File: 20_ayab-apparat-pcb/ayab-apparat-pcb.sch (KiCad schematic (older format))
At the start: 1 part

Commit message: added atmega schematic
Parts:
- removed IC?: ATMEGA328-P, DIL28, symbol ATMEGA328-P
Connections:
- wire segments 0 -> 5
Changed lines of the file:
@@
 $Descr A4 11693 8268
 encoding utf-8
-Sheet 1 2
+Sheet 1 3
 Title ""
 Date ""
@@
 Comment4 ""
 $EndDescr
-$Comp
-L ATMEGA328-P IC?
-U 1 1 52E1499B
-P 3050 2700
-F 0 "IC?" H 2300 3950 40  0000 L BNN
-F 1 "ATMEGA328-P" H 3450 1300 40  0000 L BNN
-F 2 "DIL28" H 3050 2700 30  0000 C CIN
-F 3 "" H 3050 2700 60  0000 C CNN
-	1    3050 2700
-	1    0    0    -1
-$EndComp
 $Sheet
-S 7750 3300 1200 900
+S 4600 2050 950  1050
 U 52E14CBB
 F0 "machine_interface" 50
 F1 "machine_interface.sch" 50
-F2 "EOL_L" I L 7750 3650 60
+F2 "EOL_L" I L 4600 2900 60
+F3 "SDA" I L 4600 2150 60
+F4 "SCL" I L 4600 2250 60
+F5 "EOL_R" I L 4600 3000 60
+F6 "BELTSHIFT" I L 4600 2750 60
+F7 "V1" I L 4600 2550 60
+F8 "V2" I L 4600 2650 60
 $EndSheet
+$Sheet
+S 3250 2100 800  900
+U 52E804E1
+F0 "atmega" 50
+F1 "atmega.sch" 50
+F2 "V2" I R 4050 2650 60
+F3 "V1" I R 4050 2550 60
+F4 "BELTSHIFT" I R 4050 2750 60
+F5 "SCL" I R 4050 2250 60
+F6 "SDA" I R 4050 2150 60
+$EndSheet
+Wire Wire Line
+	4050 2550 4600 2550
+Wire Wire Line
+	4050 2650 4600 2650
+Wire Wire Line
+	4050 2750 4600 2750
+Wire Wire Line
+	4050 2250 4600 2250
+Wire Wire Line
+	4050 2150 4600 2150
 $EndSCHEMATC

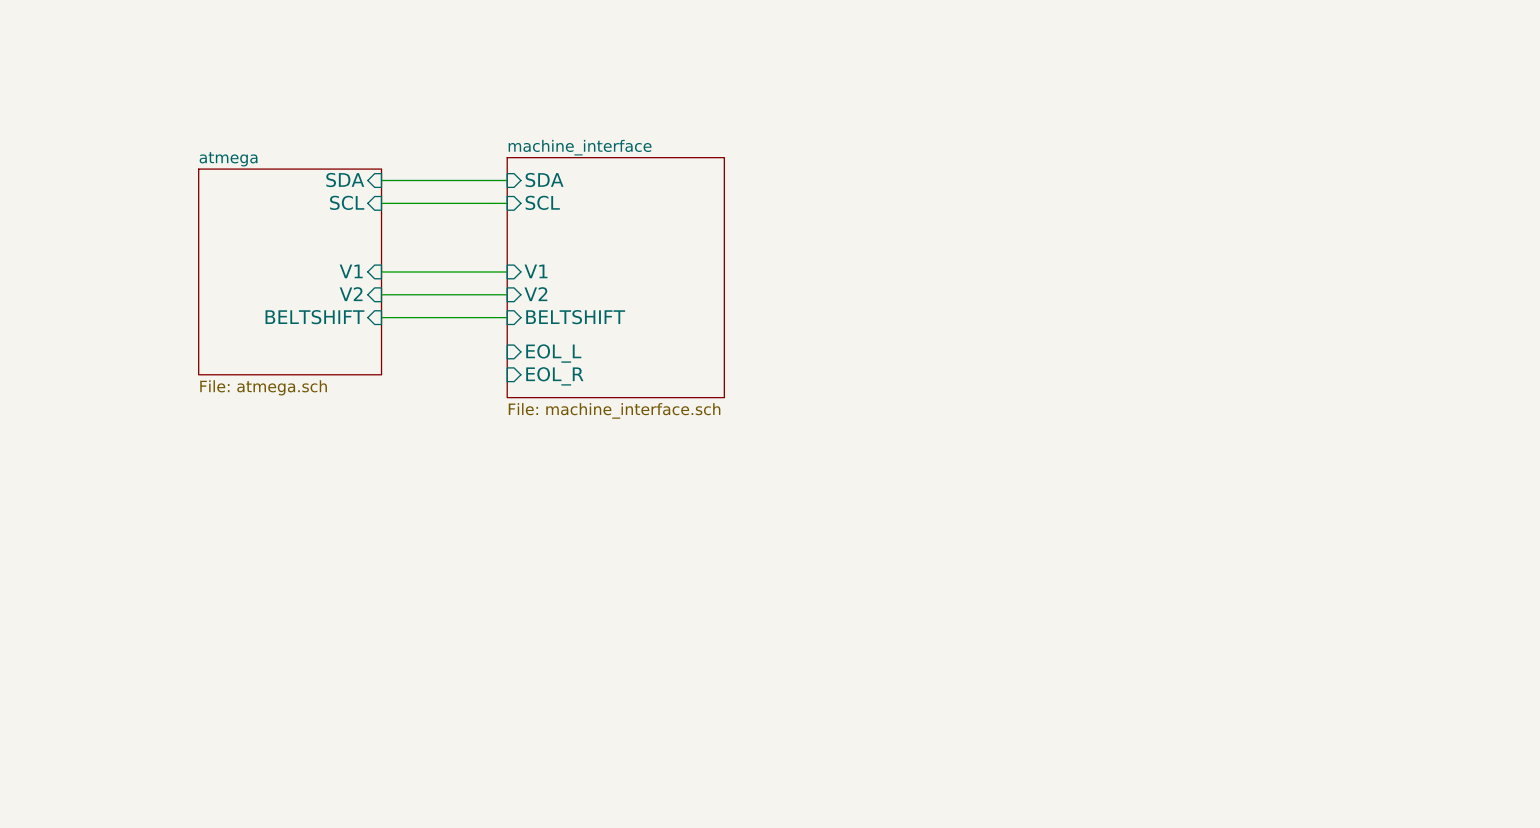
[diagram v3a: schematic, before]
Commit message: schematic structure finished -> todo add part values
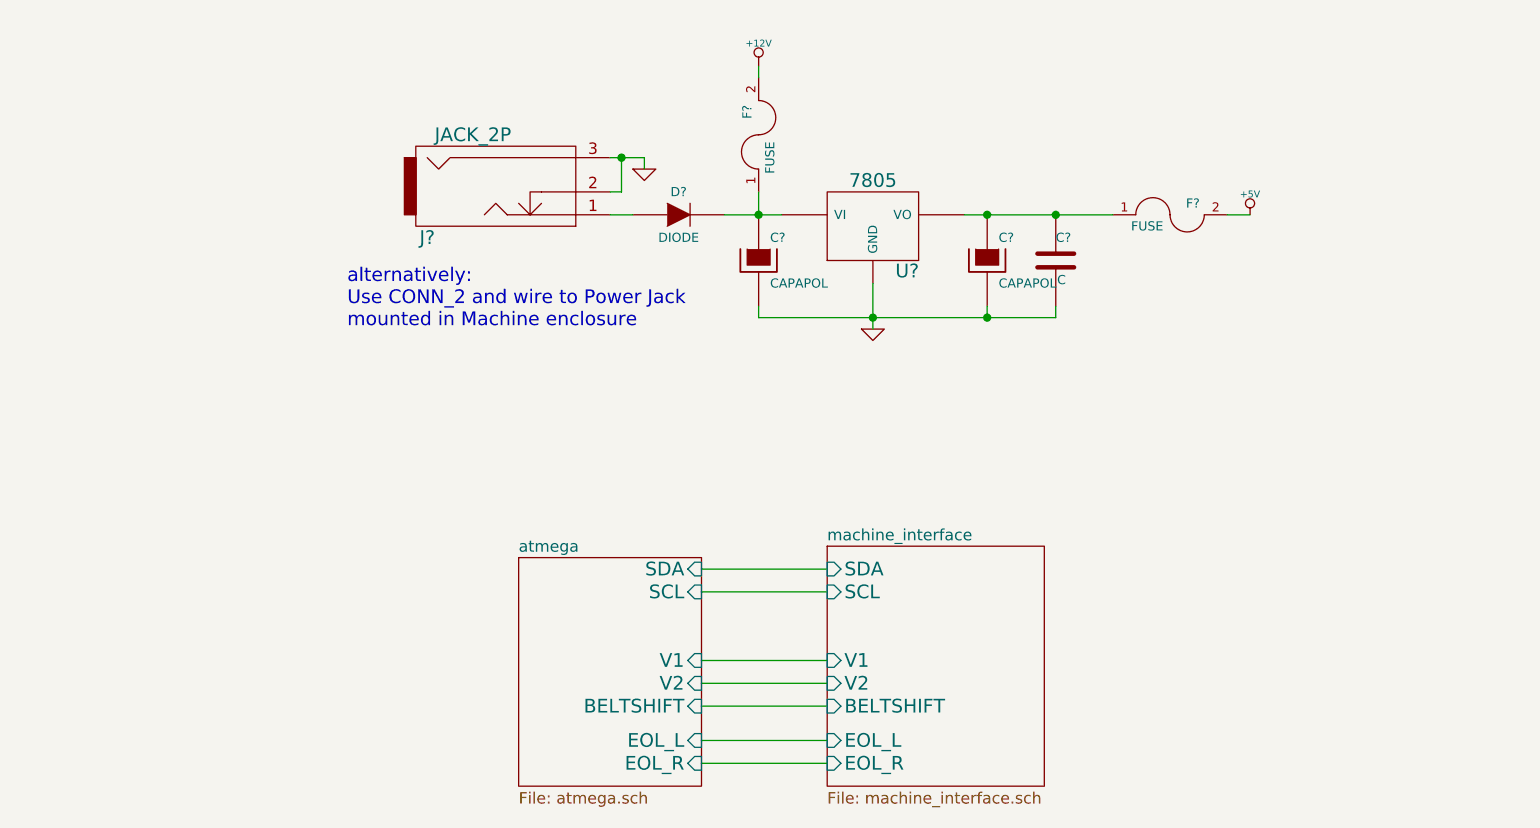
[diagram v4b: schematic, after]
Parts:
- added C? (x2): CAPAPOL, symbol CAPAPOL
- added C?: C, symbol C
- added D?: DIODE, symbol DIODE
- added F? (x2): FUSE, symbol FUSE
- added J?: JACK_2P, symbol JACK_2P
- added U?: 7805, symbol 7805
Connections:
- new net: D?.1 (A), J?.1
- new net: C?.1, D?.2 (K), F?.1, U?.VI
- new net: C?.1, C?.1, F?.1, U?.VO
- new net +12V: F?.2
- new net +5V: F?.2
- new net GND: C?.2, C?.2, C?.2, J?.2, J?.3, U?.GND
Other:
- note added: "alternatively:\nUse CONN_2 and wire to Power Jack\nmounted in Machine enclosure"
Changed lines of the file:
@@
 $EndDescr
 $Sheet
-S 4600 2050 950  1050
+S 6000 3750 950  1050
 U 52E14CBB
 F0 "machine_interface" 50
 F1 "machine_interface.sch" 50
-F2 "EOL_L" I L 4600 2900 60
-F3 "SDA" I L 4600 2150 60
-F4 "SCL" I L 4600 2250 60
-F5 "EOL_R" I L 4600 3000 60
-F6 "BELTSHIFT" I L 4600 2750 60
-F7 "V1" I L 4600 2550 60
-F8 "V2" I L 4600 2650 60
+F2 "EOL_L" I L 6000 4600 60
+F3 "SDA" I L 6000 3850 60
+F4 "SCL" I L 6000 3950 60
+F5 "EOL_R" I L 6000 4700 60
+F6 "BELTSHIFT" I L 6000 4450 60
+F7 "V1" I L 6000 4250 60
+F8 "V2" I L 6000 4350 60
 $EndSheet
 $Sheet
-S 3250 2100 800  900
+S 4650 3800 800  1000
 U 52E804E1
 F0 "atmega" 50
 F1 "atmega.sch" 50
-F2 "V2" I R 4050 2650 60
-F3 "V1" I R 4050 2550 60
-F4 "BELTSHIFT" I R 4050 2750 60
-F5 "SCL" I R 4050 2250 60
-F6 "SDA" I R 4050 2150 60
+F2 "V2" I R 5450 4350 60
+F3 "V1" I R 5450 4250 60
+F4 "BELTSHIFT" I R 5450 4450 60
+F5 "SCL" I R 5450 3950 60
+F6 "SDA" I R 5450 3850 60
+F7 "EOL_R" I R 5450 4700 60
+F8 "EOL_L" I R 5450 4600 60
 $EndSheet
 Wire Wire Line
-	4050 2550 4600 2550
-Wire Wire Line
-	4050 2650 4600 2650
-Wire Wire Line
-	4050 2750 4600 2750
-Wire Wire Line
-	4050 2250 4600 2250
-Wire Wire Line
-	4050 2150 4600 2150
+	5450 4250 6000 4250
+Wire Wire Line
+	5450 4350 6000 4350
+Wire Wire Line
+	5450 4450 6000 4450
+Wire Wire Line
+	5450 3950 6000 3950
+Wire Wire Line
+	5450 3850 6000 3850
+Wire Wire Line
+	5450 4600 6000 4600
+Wire Wire Line
+	5450 4700 6000 4700
+$Comp
+L JACK_2P J?
+U 1 1 52EAACEF
+P 4600 2200
+F 0 "J?" H 4250 2000 60  0000 C CNN
+F 1 "JACK_2P" H 4450 2450 60  0000 C CNN
+F 2 "" H 4600 2200 60  0000 C CNN
+F 3 "" H 4600 2200 60  0000 C CNN
+	1    4600 2200
+	1    0    0    -1
+$EndComp
+$Comp
+L CAPAPOL C?
+U 1 1 52EAB7DE
+P 5700 2500
+F 0 "C?" H 5750 2600 40  0000 L CNN
+F 1 "CAPAPOL" H 5750 2400 40  0000 L CNN
+F 2 "" H 5800 2350 30  0000 C CNN
+F 3 "" H 5700 2500 300 0000 C CNN
+	1    5700 2500
+	1    0    0    -1
+$EndComp
+$Comp
+L 7805 U?
+U 1 1 52EAB846
+P 6200 2350
+F 0 "U?" H 6350 2154 60  0000 C CNN
+F 1 "7805" H 6200 2550 60  0000 C CNN
+F 2 "" H 6200 2350 60  0000 C CNN
+F 3 "" H 6200 2350 60  0000 C CNN
+	1    6200 2350
+	1    0    0    -1
+$EndComp
+$Comp
+L CAPAPOL C?
+U 1 1 52EAB85A
+P 6700 2500
+F 0 "C?" H 6750 2600 40  0000 L CNN
+F 1 "CAPAPOL" H 6750 2400 40  0000 L CNN
+F 2 "" H 6800 2350 30  0000 C CNN
+F 3 "" H 6700 2500 300 0000 C CNN
+	1    6700 2500
+	1    0    0    -1
+$EndComp
+$Comp
+L DIODE D?
+U 1 1 52EAB86E
+P 5350 2300
+F 0 "D?" H 5350 2400 40  0000 C CNN
+F 1 "DIODE" H 5350 2200 40  0000 C CNN
+F 2 "" H 5350 2300 60  0000 C CNN
+F 3 "" H 5350 2300 60  0000 C CNN
+	1    5350 2300
+	1    0    0    -1
+$EndComp
+Wire Wire Line
+	5050 2200 5100 2200
+Wire Wire Line
+	5100 2200 5100 2050
+Wire Wire Line
+	5050 2050 5200 2050
+Wire Wire Line
+	5050 2300 5150 2300
+$Comp
+L GND #PWR?
+U 1 1 52EAB978
+P 5200 2100
+F 0 "#PWR?" H 5200 2100 30  0001 C CNN
+F 1 "GND" H 5200 2030 30  0001 C CNN
+F 2 "" H 5200 2100 60  0000 C CNN
+F 3 "" H 5200 2100 60  0000 C CNN
+	1    5200 2100
+	1    0    0    -1
+$EndComp
+Wire Wire Line
+	5200 2050 5200 2100
+Connection ~ 5100 2050
+Wire Wire Line
+	5550 2300 5800 2300
+Wire Wire Line
+	6600 2300 7250 2300
+Wire Wire Line
+	6700 2700 6700 2750
+Wire Wire Line
+	5700 2750 7000 2750
+Wire Wire Line
+	5700 2750 5700 2700
+$Comp
+L GND #PWR?
+U 1 1 52EABC97
+P 6200 2800
+F 0 "#PWR?" H 6200 2800 30  0001 C CNN
+F 1 "GND" H 6200 2730 30  0001 C CNN
+F 2 "" H 6200 2800 60  0000 C CNN
+F 3 "" H 6200 2800 60  0000 C CNN
+	1    6200 2800
+	1    0    0    -1
+$EndComp
+Wire Wire Line
+	6200 2600 6200 2800
+Connection ~ 6200 2750
+$Comp
+L C C?
+U 1 1 52EAC19E
+P 7000 2500
+F 0 "C?" H 7000 2600 40  0000 L CNN
+F 1 "C" H 7006 2415 40  0000 L CNN
+F 2 "" H 7038 2350 30  0000 C CNN
+F 3 "" H 7000 2500 60  0000 C CNN
+	1    7000 2500
+	1    0    0    -1
+$EndComp
+Connection ~ 6700 2300
+Connection ~ 7000 2300
+Wire Wire Line
+	7000 2750 7000 2700
+Connection ~ 6700 2750
+$Comp
+L +5V #PWR?
+U 1 1 52EAC279
+P 7850 2300
+F 0 "#PWR?" H 7850 2390 20  0001 C CNN
+F 1 "+5V" H 7850 2390 30  0000 C CNN
+F 2 "" H 7850 2300 60  0000 C CNN
+F 3 "" H 7850 2300 60  0000 C CNN
+	1    7850 2300
+	1    0    0    -1
+$EndComp
+$Comp
+L +12V #PWR?
+U 1 1 52EAEFAF
+P 5700 1650
+F 0 "#PWR?" H 5700 1600 20  0001 C CNN
+F 1 "+12V" H 5700 1750 30  0000 C CNN
+F 2 "" H 5700 1650 60  0000 C CNN
+F 3 "" H 5700 1650 60  0000 C CNN
+	1    5700 1650
+	1    0    0    -1
+$EndComp
+$Comp
+L FUSE F?
+U 1 1 52EAEFC3
+P 7500 2300
+F 0 "F?" H 7600 2350 40  0000 C CNN
+F 1 "FUSE" H 7400 2250 40  0000 C CNN
+F 2 "" H 7500 2300 60  0000 C CNN
+F 3 "" H 7500 2300 60  0000 C CNN
+	1    7500 2300
+	1    0    0    -1
+$EndComp
+Wire Wire Line
+	7750 2300 7850 2300
+$Comp
+L FUSE F?
+U 1 1 52EAF592
+P 5700 1950
+F 0 "F?" H 5800 2000 40  0000 C CNN
+F 1 "FUSE" H 5600 1900 40  0000 C CNN
+F 2 "" H 5700 1950 60  0000 C CNN
+F 3 "" H 5700 1950 60  0000 C CNN
+	1    5700 1950
+	0    -1   -1   0
+$EndComp
+Wire Wire Line
+	5700 2300 5700 2200
+Connection ~ 5700 2300
+Wire Wire Line
+	5700 1700 5700 1650
+Text Notes 3900 2800 0    60   ~ 0
+alternatively:\nUse CONN_2 and wire to Power Jack\nmounted in Machine enclosure
 $EndSCHEMATC

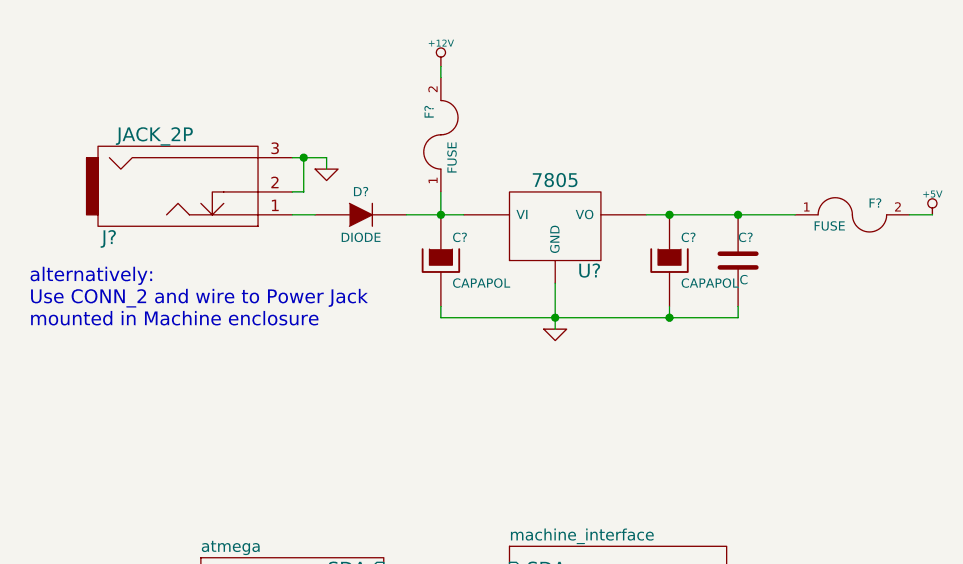
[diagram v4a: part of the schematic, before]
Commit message: added partnames and values, generated first version of netlist, ready to assign footprints
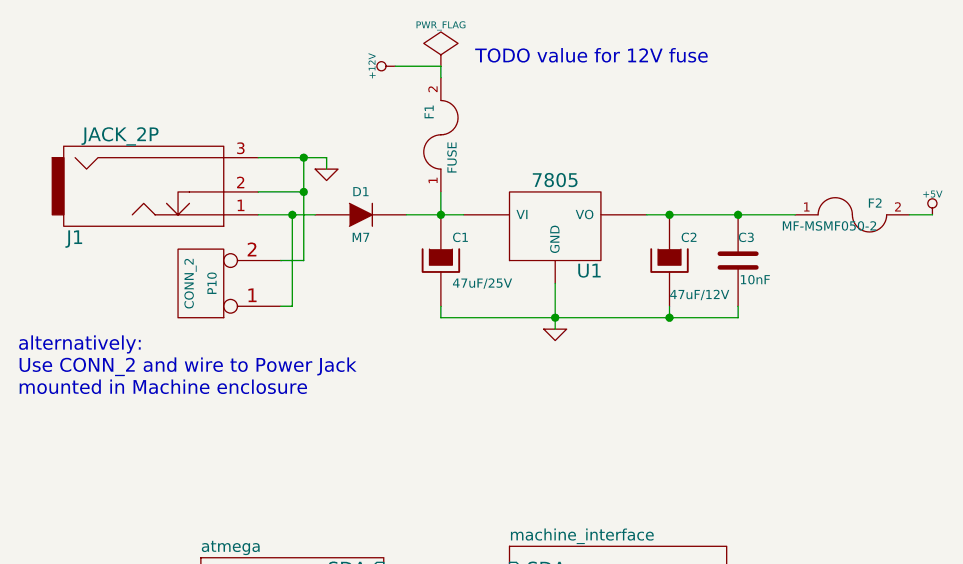
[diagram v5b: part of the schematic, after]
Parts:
- added P10: CONN_2, symbol CONN_2
- C1: renamed from C?; value CAPAPOL -> 47uF/25V
- C2: renamed from C?; value CAPAPOL -> 47uF/12V
- C3: renamed from C?; value C -> 10nF
- D1: renamed from D?; value DIODE -> M7
- F2: renamed from F?; value FUSE -> MF-MSMF050-2
- gave numbers to parts that had none: 3
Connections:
- net GND: now also P10.2 (PM)
- net at D1.1 (A), J1.1: now also P10.1 (P1)
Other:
- note added: "TODO value for 12V fuse"
- moved on the sheet: J1
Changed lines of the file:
@@
 	5450 4700 6000 4700
 $Comp
-L JACK_2P J?
+L JACK_2P J1
 U 1 1 52EAACEF
-P 4600 2200
-F 0 "J?" H 4250 2000 60  0000 C CNN
-F 1 "JACK_2P" H 4450 2450 60  0000 C CNN
-F 2 "" H 4600 2200 60  0000 C CNN
-F 3 "" H 4600 2200 60  0000 C CNN
-	1    4600 2200
-	1    0    0    -1
-$EndComp
-$Comp
-L CAPAPOL C?
+P 4450 2200
+F 0 "J1" H 4100 2000 60  0000 C CNN
+F 1 "JACK_2P" H 4300 2450 60  0000 C CNN
+F 2 "" H 4450 2200 60  0000 C CNN
+F 3 "" H 4450 2200 60  0000 C CNN
+	1    4450 2200
+	1    0    0    -1
+$EndComp
+$Comp
+L CAPAPOL C1
 U 1 1 52EAB7DE
 P 5700 2500
-F 0 "C?" H 5750 2600 40  0000 L CNN
-F 1 "CAPAPOL" H 5750 2400 40  0000 L CNN
+F 0 "C1" H 5750 2600 40  0000 L CNN
+F 1 "47uF/25V" H 5750 2400 40  0000 L CNN
 F 2 "" H 5800 2350 30  0000 C CNN
 F 3 "" H 5700 2500 300 0000 C CNN
@@
 $EndComp
 $Comp
-L 7805 U?
+L 7805 U1
 U 1 1 52EAB846
 P 6200 2350
-F 0 "U?" H 6350 2154 60  0000 C CNN
+F 0 "U1" H 6350 2154 60  0000 C CNN
 F 1 "7805" H 6200 2550 60  0000 C CNN
 F 2 "" H 6200 2350 60  0000 C CNN
@@
 $EndComp
 $Comp
-L CAPAPOL C?
+L CAPAPOL C2
 U 1 1 52EAB85A
 P 6700 2500
-F 0 "C?" H 6750 2600 40  0000 L CNN
-F 1 "CAPAPOL" H 6750 2400 40  0000 L CNN
+F 0 "C2" H 6750 2600 40  0000 L CNN
+F 1 "47uF/12V" H 6700 2350 40  0000 L CNN
 F 2 "" H 6800 2350 30  0000 C CNN
 F 3 "" H 6700 2500 300 0000 C CNN
@@
 $EndComp
 $Comp
-L DIODE D?
+L DIODE D1
 U 1 1 52EAB86E
 P 5350 2300
-F 0 "D?" H 5350 2400 40  0000 C CNN
-F 1 "DIODE" H 5350 2200 40  0000 C CNN
+F 0 "D1" H 5350 2400 40  0000 C CNN
+F 1 "M7" H 5350 2200 40  0000 C CNN
 F 2 "" H 5350 2300 60  0000 C CNN
 F 3 "" H 5350 2300 60  0000 C CNN
@@
 $EndComp
 Wire Wire Line
-	5050 2200 5100 2200
-Wire Wire Line
-	5100 2200 5100 2050
-Wire Wire Line
-	5050 2050 5200 2050
-Wire Wire Line
-	5050 2300 5150 2300
-$Comp
-L GND #PWR?
+	4900 2200 5100 2200
+Wire Wire Line
+	5100 2050 5100 2500
+Wire Wire Line
+	4900 2050 5200 2050
+Wire Wire Line
+	4900 2300 5150 2300
+$Comp
+L GND #PWR01
 U 1 1 52EAB978
 P 5200 2100
-F 0 "#PWR?" H 5200 2100 30  0001 C CNN
+F 0 "#PWR01" H 5200 2100 30  0001 C CNN
 F 1 "GND" H 5200 2030 30  0001 C CNN
 F 2 "" H 5200 2100 60  0000 C CNN
@@
 	6600 2300 7250 2300
 Wire Wire Line
-	6700 2700 6700 2750
+	6700 2750 6700 2700
 Wire Wire Line
 	5700 2750 7000 2750
@@
 	5700 2750 5700 2700
 $Comp
-L GND #PWR?
+L GND #PWR02
 U 1 1 52EABC97
 P 6200 2800
-F 0 "#PWR?" H 6200 2800 30  0001 C CNN
+F 0 "#PWR02" H 6200 2800 30  0001 C CNN
 F 1 "GND" H 6200 2730 30  0001 C CNN
 F 2 "" H 6200 2800 60  0000 C CNN
@@
 Connection ~ 6200 2750
 $Comp
-L C C?
+L C C3
 U 1 1 52EAC19E
 P 7000 2500
-F 0 "C?" H 7000 2600 40  0000 L CNN
-F 1 "C" H 7006 2415 40  0000 L CNN
+F 0 "C3" H 7000 2600 40  0000 L CNN
+F 1 "10nF" H 7006 2415 40  0000 L CNN
 F 2 "" H 7038 2350 30  0000 C CNN
 F 3 "" H 7000 2500 60  0000 C CNN
@@
 Connection ~ 6700 2750
 $Comp
-L +5V #PWR?
+L +5V #PWR03
 U 1 1 52EAC279
 P 7850 2300
-F 0 "#PWR?" H 7850 2390 20  0001 C CNN
+F 0 "#PWR03" H 7850 2390 20  0001 C CNN
 F 1 "+5V" H 7850 2390 30  0000 C CNN
 F 2 "" H 7850 2300 60  0000 C CNN
@@
 $EndComp
 $Comp
-L +12V #PWR?
+L +12V #PWR04
 U 1 1 52EAEFAF
-P 5700 1650
-F 0 "#PWR?" H 5700 1600 20  0001 C CNN
-F 1 "+12V" H 5700 1750 30  0000 C CNN
-F 2 "" H 5700 1650 60  0000 C CNN
-F 3 "" H 5700 1650 60  0000 C CNN
-	1    5700 1650
-	1    0    0    -1
-$EndComp
-$Comp
-L FUSE F?
+P 5500 1650
+F 0 "#PWR04" H 5500 1600 20  0001 C CNN
+F 1 "+12V" H 5500 1750 30  0000 C CNN
+F 2 "" H 5500 1650 60  0000 C CNN
+F 3 "" H 5500 1650 60  0000 C CNN
+	1    5500 1650
+	0    -1   -1   0
+$EndComp
+$Comp
+L FUSE F2
 U 1 1 52EAEFC3
 P 7500 2300
-F 0 "F?" H 7600 2350 40  0000 C CNN
-F 1 "FUSE" H 7400 2250 40  0000 C CNN
+F 0 "F2" H 7600 2350 40  0000 C CNN
+F 1 "MF-MSMF050-2" H 7400 2250 40  0000 C CNN
 F 2 "" H 7500 2300 60  0000 C CNN
 F 3 "" H 7500 2300 60  0000 C CNN
@@
 	7750 2300 7850 2300
 $Comp
-L FUSE F?
+L FUSE F1
 U 1 1 52EAF592
 P 5700 1950
-F 0 "F?" H 5800 2000 40  0000 C CNN
+F 0 "F1" H 5800 2000 40  0000 C CNN
 F 1 "FUSE" H 5600 1900 40  0000 C CNN
 F 2 "" H 5700 1950 60  0000 C CNN
@@
 	5700 2300 5700 2200
 Connection ~ 5700 2300
+Text Notes 3850 3100 0    60   ~ 0
+alternatively:\nUse CONN_2 and wire to Power Jack\nmounted in Machine enclosure
+$Comp
+L CONN_2 P10
+U 1 1 52EEC1AF
+P 4650 2600
+F 0 "P10" V 4600 2600 40  0000 C CNN
+F 1 "CONN_2" V 4700 2600 40  0000 C CNN
+F 2 "" H 4650 2600 60  0000 C CNN
+F 3 "" H 4650 2600 60  0000 C CNN
+	1    4650 2600
+	-1   0    0    1
+$EndComp
+Connection ~ 5100 2200
+Wire Wire Line
+	5100 2500 5000 2500
+Wire Wire Line
+	5000 2700 5050 2700
+Wire Wire Line
+	5050 2700 5050 2300
+Connection ~ 5050 2300
+Text Notes 5850 1650 0    60   ~ 0
+TODO value for 12V fuse
 Wire Wire Line
 	5700 1700 5700 1650
-Text Notes 3900 2800 0    60   ~ 0
-alternatively:\nUse CONN_2 and wire to Power Jack\nmounted in Machine enclosure
+Wire Wire Line
+	5700 1650 5500 1650
+$Comp
+L PWR_FLAG #FLG05
+U 1 1 52EECA32
+P 5700 1650
+F 0 "#FLG05" H 5700 1745 30  0001 C CNN
+F 1 "PWR_FLAG" H 5700 1830 30  0000 C CNN
+F 2 "" H 5700 1650 60  0000 C CNN
+F 3 "" H 5700 1650 60  0000 C CNN
+	1    5700 1650
+	1    0    0    -1
+$EndComp
 $EndSCHEMATC
